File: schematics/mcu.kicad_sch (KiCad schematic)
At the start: 3 parts, among them SW1 SW_SPST, U1 ESP32-C3-WROOM-02

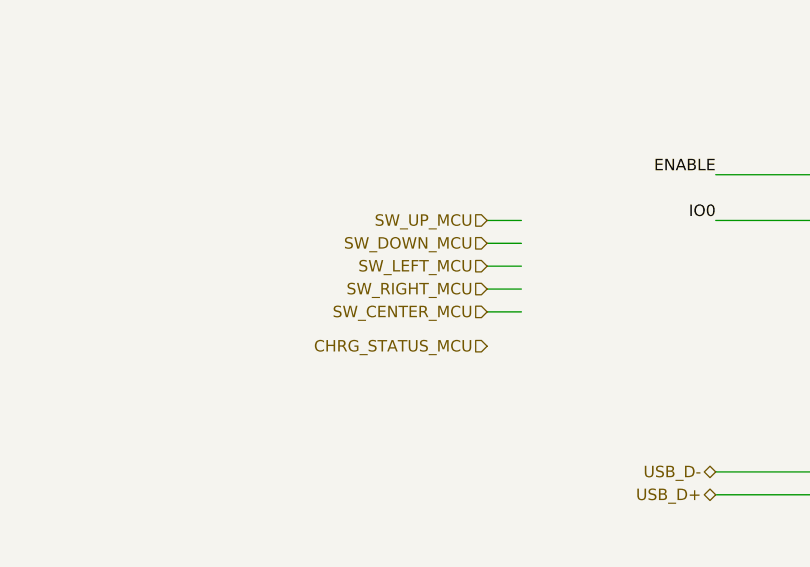
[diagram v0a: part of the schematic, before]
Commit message: Make square
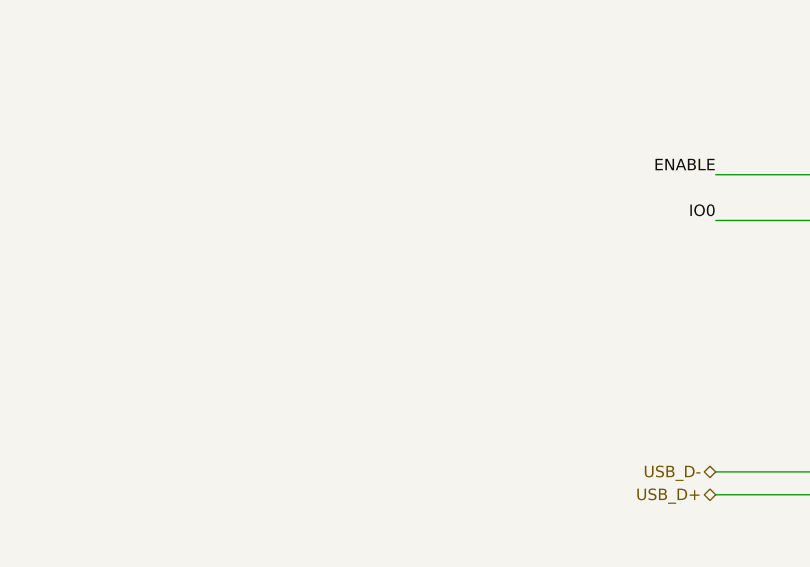
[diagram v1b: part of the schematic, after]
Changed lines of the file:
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@@
-	(wire
-		(pts
-			(xy 88.9 97.79) (xy 92.71 97.79)
-		)
-		(stroke
-			(width 0)
-			(type default)
-		)
-	)
 	(wire
 		(pts
 			(xy 114.3 87.63) (xy 125.73 87.63)
-		)
-		(stroke
-			(width 0)
-			(type default)
-		)
-	)
-	(wire
-		(pts
-			(xy 88.9 95.25) (xy 92.71 95.25)
 		)
 		(stroke
@@
 	(wire
 		(pts
-			(xy 88.9 87.63) (xy 92.71 87.63)
-		)
-		(stroke
-			(width 0)
-			(type default)
-		)
-	)
-	(wire
-		(pts
 			(xy 22.86 36.83) (xy 22.86 43.18)
-		)
-		(stroke
-			(width 0)
-			(type default)
-		)
-	)
-	(wire
-		(pts
-			(xy 88.9 92.71) (xy 92.71 92.71)
 		)
 		(stroke
@@
 		(pts
 			(xy 36.83 25.4) (xy 36.83 27.94)
-		)
-		(stroke
-			(width 0)
-			(type default)
-		)
-	)
-	(wire
-		(pts
-			(xy 88.9 90.17) (xy 92.71 90.17)
 		)
 		(stroke
@@
 		)
 	)
-	(hierarchical_label "SW_DOWN_MCU"
-		(shape input)
-		(at 88.9 90.17 180)
-		(effects
-			(font
-				(size 1.27 1.27)
-			)
-			(justify right)
-		)
-	)
 	(hierarchical_label "USB_D+"
 		(shape bidirectional)
@@
 		(effects
 			(font
-				(size 1.27 1.27)
-			)
-			(justify right)
-		)
-	)
-	(hierarchical_label "SW_CENTER_MCU"
-		(shape input)
-		(at 88.9 97.79 180)
-		(effects
-			(font
-				(size 1.27 1.27)
-			)
-			(justify right)
-		)
-	)
-	(hierarchical_label "SW_RIGHT_MCU"
-		(shape input)
-		(at 88.9 95.25 180)
-		(effects
-			(font
-				(size 1.27 1.27)
-			)
-			(justify right)
-		)
-	)
-	(hierarchical_label "SW_UP_MCU"
-		(shape input)
-		(at 88.9 87.63 180)
-		(effects
-			(font
-				(size 1.27 1.27)
-			)
-			(justify right)
-		)
-	)
-	(hierarchical_label "SW_LEFT_MCU"
-		(shape input)
-		(at 88.9 92.71 180)
-		(effects
-			(font
-				(size 1.27 1.27)
-			)
-			(justify right)
-		)
-	)
-	(hierarchical_label "CHRG_STATUS_MCU"
-		(shape input)
-		(at 88.9 101.6 180)
-		(effects
-			(font

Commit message: Update README
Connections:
- net SDA_MCU: now reaches U1.7 (IO8)
- net SCL_MCU: now reaches U1.8 (IO9)
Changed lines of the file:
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@@
+	(wire
+		(pts
+			(xy 114.3 107.95) (xy 125.73 107.95)
+		)
+		(stroke
+			(width 0)
+			(type default)
+		)
+	)
 	(wire
 		(pts
@@
 		)
 	)
+	(wire
+		(pts
+			(xy 114.3 110.49) (xy 125.73 110.49)
+		)
+		(stroke
+			(width 0)
+			(type default)
+		)
+	)
 	(label "ENABLE"
 		(at 114.3 82.55 180)
@@
 		(effects
 			(font
+				(size 1.27 1.27)
+			)
+			(justify right)
+		)
+	)
+	(hierarchical_label "SCL_MCU"
+		(shape bidirectional)
+		(at 114.3 110.49 180)
+		(effects
+			(font
+				(size 1.27 1.27)
+			)
+			(justify right)
+		)
+	)
+	(hierarchical_label "SDA_MCU"
+		(shape bidirectional)
+		(at 114.3 107.95 180)
+		(effects
+			(font
+				(size 1.27 1.27)
+			)
+			(justify right)
+		)
+	)
+	(hierarchical_label "LED_MCU"
+		(shape bidirectional)
+		(at 76.2 101.6 180)
+		(effects
+			(font

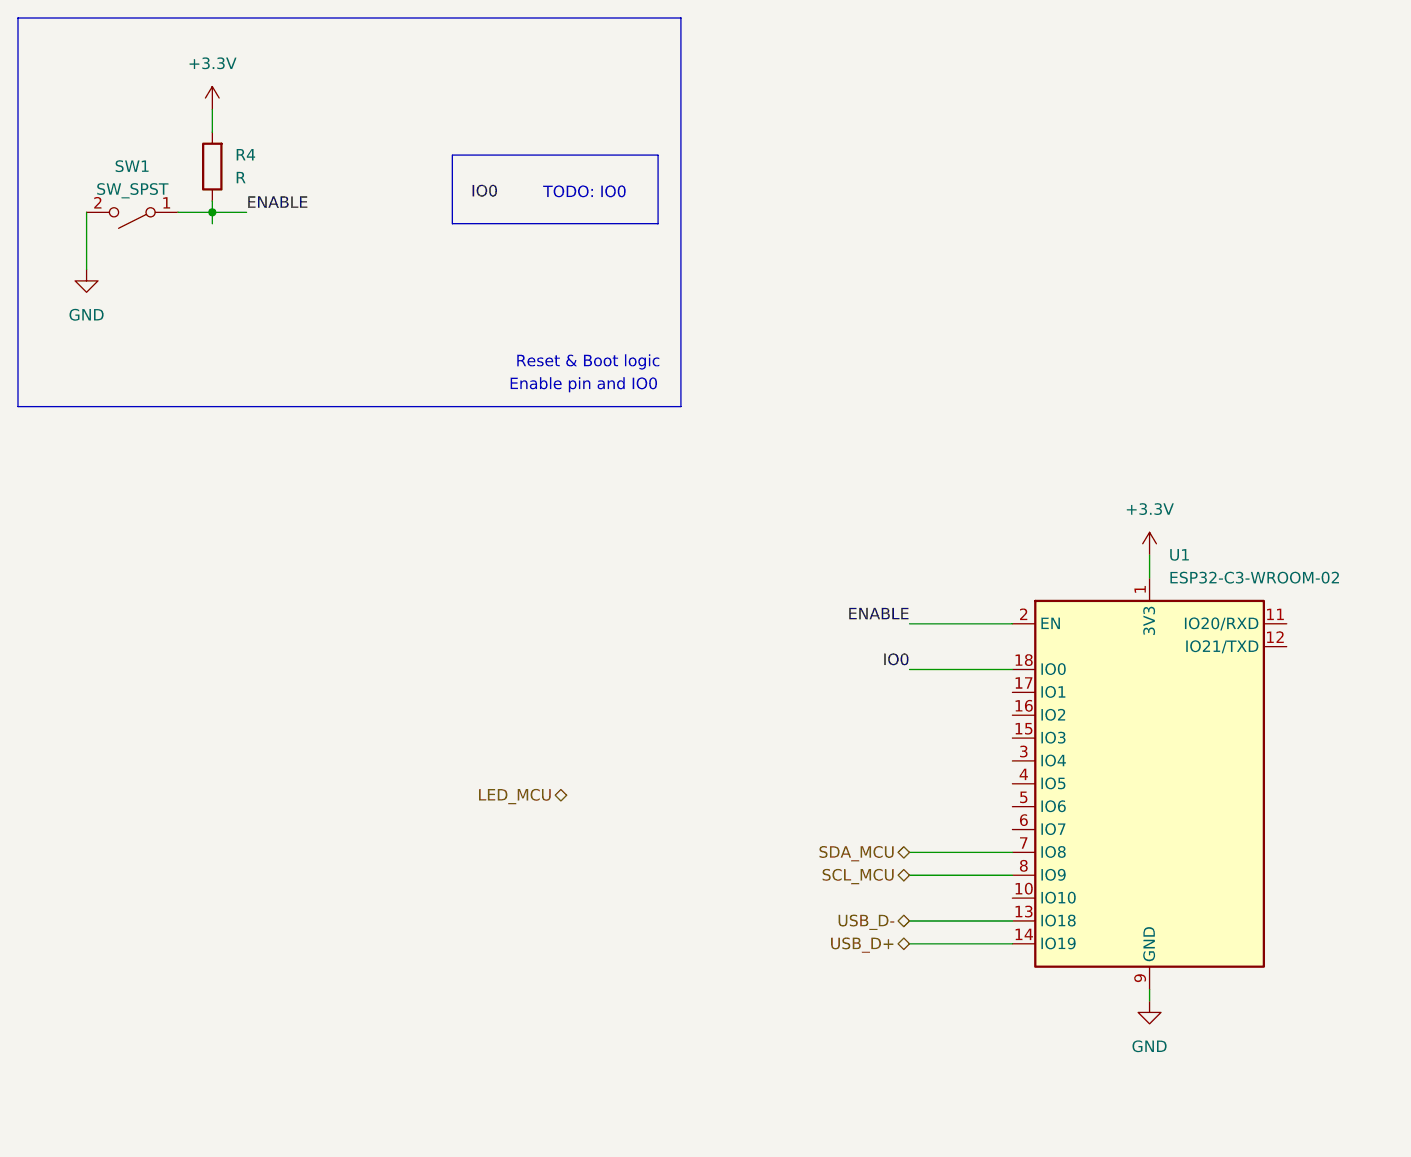
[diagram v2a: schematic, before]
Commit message: Wire buttons
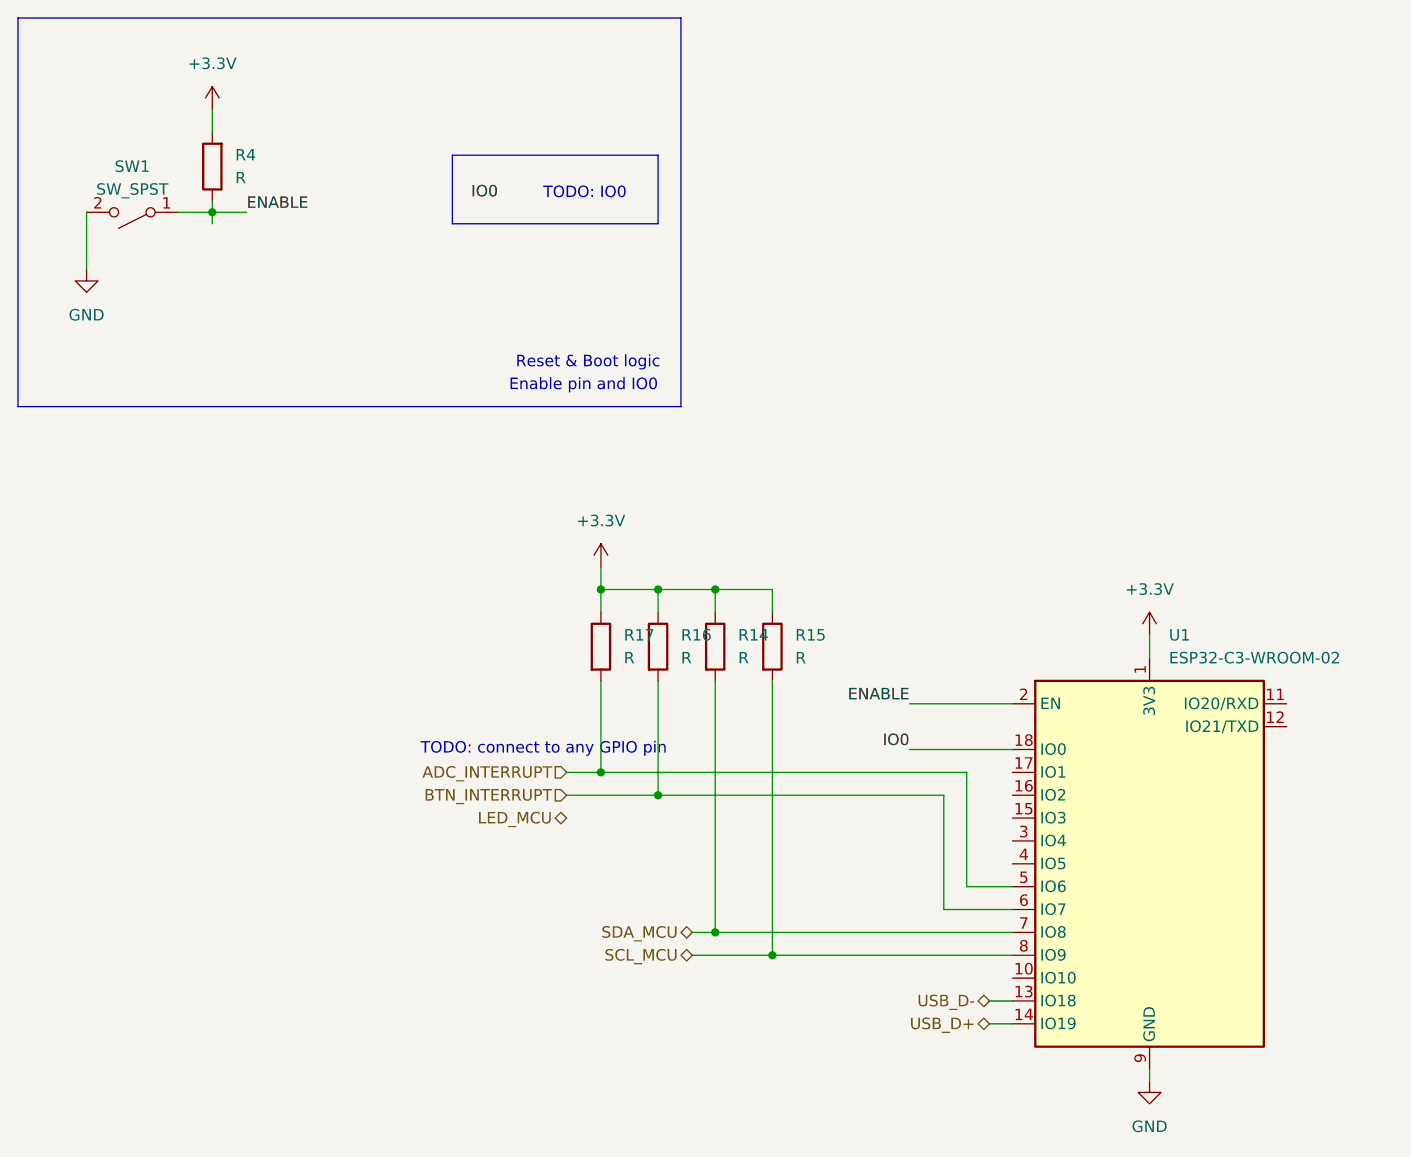
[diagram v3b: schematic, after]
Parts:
- added R14, R15, R16, R17: R, symbol Device:R
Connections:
- net +3.3V: now also R14.1, R15.1, R16.1, R17.1
- net SCL_MCU: now also R15.2
- net SDA_MCU: now also R14.2
- net ADC_INTERRUPT: now reaches U1.5 (IO6)
- net ADC_INTERRUPT: now also R17.2
- net BTN_INTERRUPT: now reaches U1.6 (IO7)
- net BTN_INTERRUPT: now also R16.2
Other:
- note added: "TODO: connect to any GPIO pin"
- moved on the sheet: U1

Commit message: Update bom
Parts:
- U1: JLCPCB (none) -> C2934560
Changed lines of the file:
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@@
+			)
+		)
+		(property "JLCPCB" "C2934560"
+			(at 140.97 109.22 0)
+			(effects
+				(font
+					(size 1.27 1.27)
+				)
+				(hide yes)
 			)
 		)

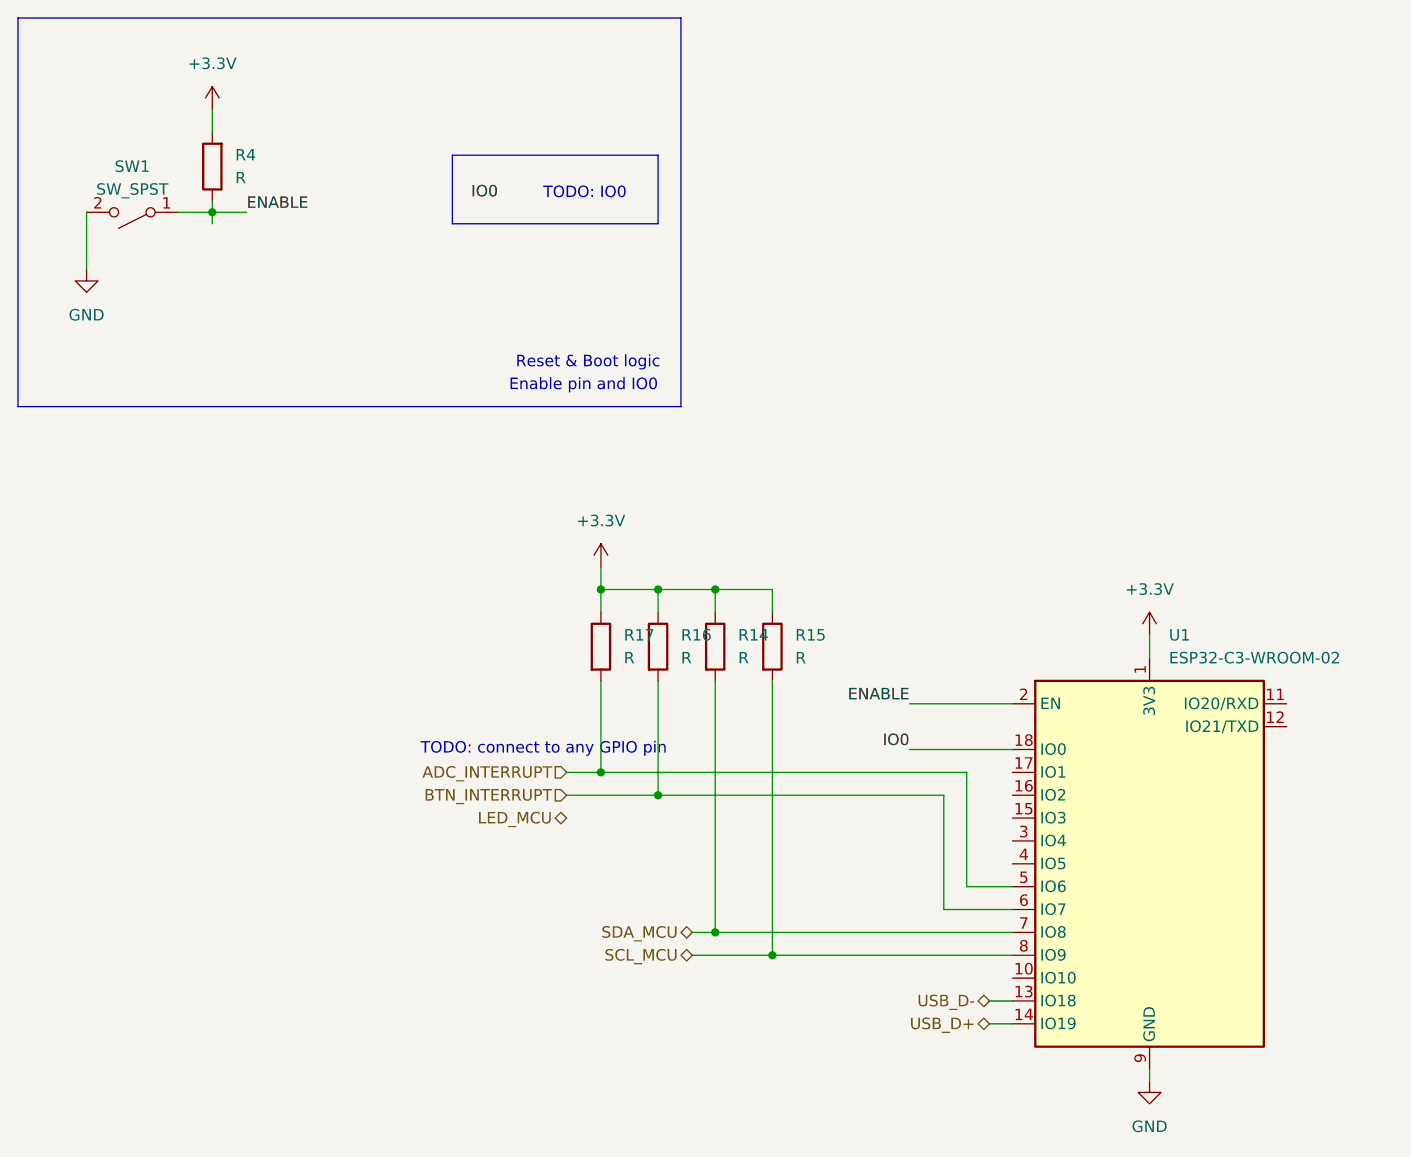
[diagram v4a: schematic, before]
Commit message: Add LED driver ic TLC59208F
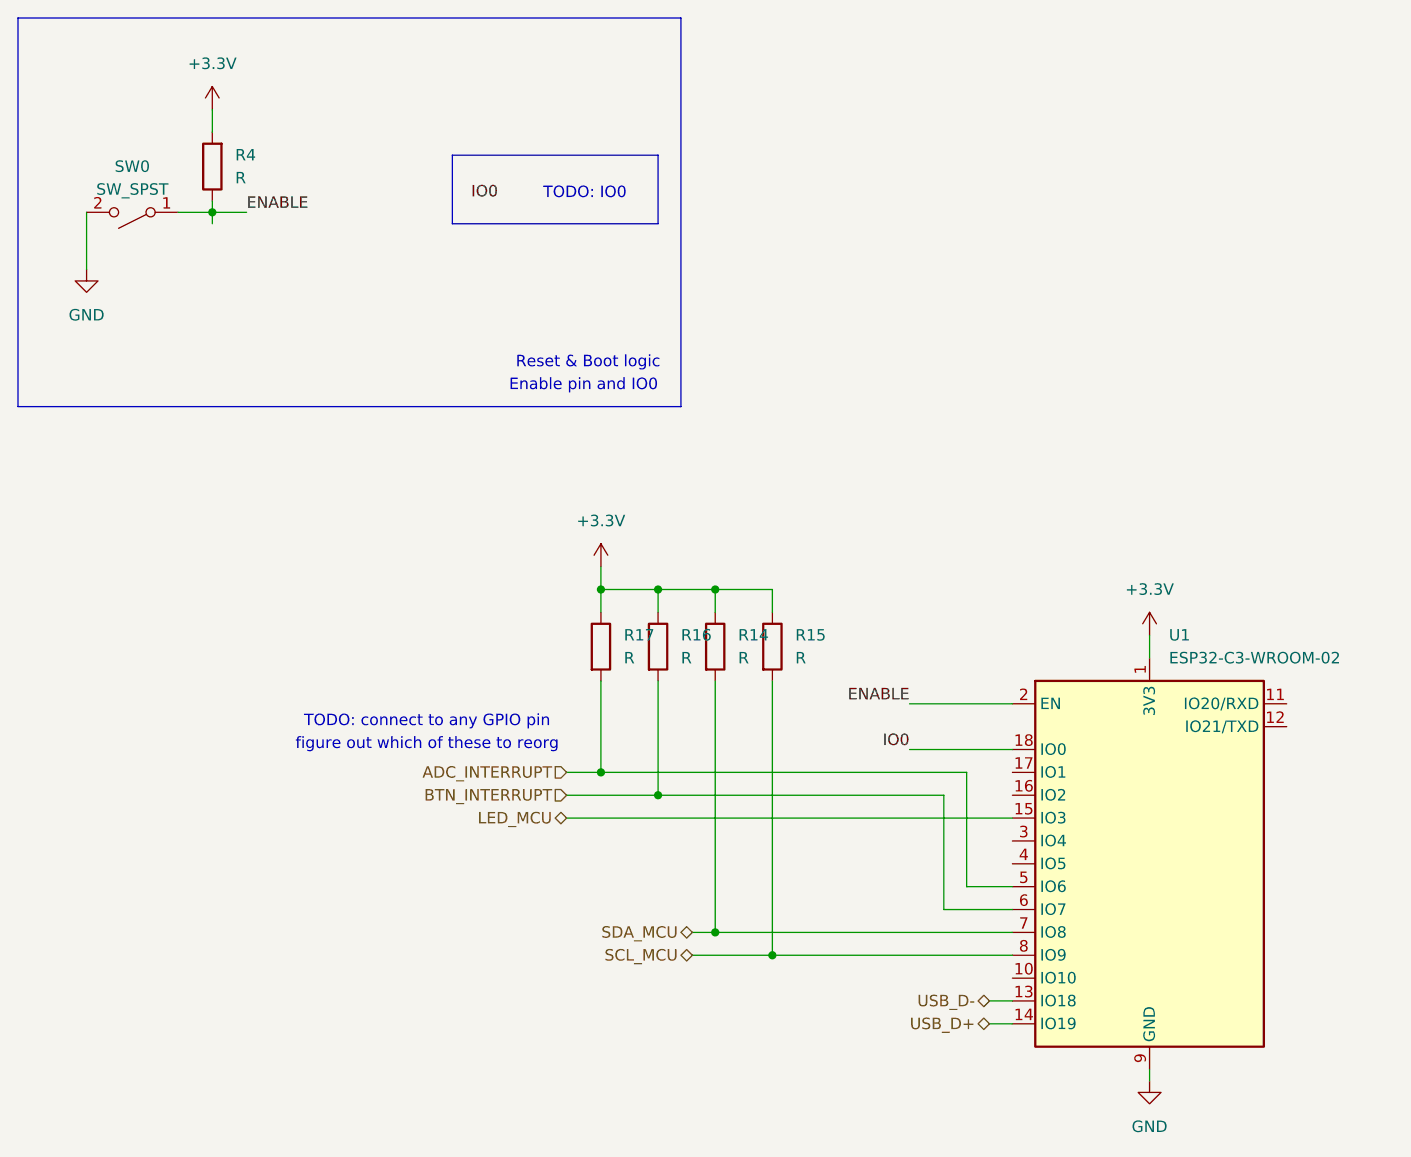
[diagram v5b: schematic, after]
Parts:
- renumbered SW1 to SW0
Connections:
- net LED_MCU: now also U1.15 (IO3)
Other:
- note added: "figure out which of these to reorg"
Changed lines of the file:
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@@
+		)
+	)
+	(text "figure out which of these to reorg"
+		(exclude_from_sim no)
+		(at 60.706 96.012 0)
+		(effects
+			(font
+				(size 1.27 1.27)
+			)
 		)
 	)
@@
 	(text "TODO: connect to any GPIO pin"
 		(exclude_from_sim no)
-		(at 73.66 96.52 0)
+		(at 60.706 93.472 0)
 		(effects
 			(font
@@
 		(pts
 			(xy 140.97 132.08) (xy 140.97 133.35)
+		)
+		(stroke
+			(width 0)
+			(type default)
+		)
+	)
+	(wire
+		(pts
+			(xy 76.2 104.14) (xy 125.73 104.14)
 		)
 		(stroke
@@
 		(dnp no)
 		(fields_autoplaced yes)
-		(property "Reference" "SW1"
+		(property "Reference" "SW0"
 			(at 27.94 31.75 0)
 			(effects
@@
 			(project "siiren"
 				(path "/f2af4cd4-99cf-4d01-92f6-6413371e0fe3/4496be08-8f2b-4c9e-be02-ccdba308cb50"
-					(reference "SW1")
+					(reference "SW0")
 					(unit 1)
 				)
